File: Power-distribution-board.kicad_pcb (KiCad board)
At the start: 2 copper layers, 137.5 x 119 mm, 98 parts, among them J1 Conn_01x03_Pin, J10 2606-1104/020-000, J11 178.6165.0001, J12 2606-1104/020-000, J14 178.6165.0001, J15 2606-1104/020-000, J16 2606-1104/020-000, J17 178.6165.0001, J18 178.6165.0001, J19 178.6165.0001, J2 2616-1102/020-000, J3 USB_C_Receptacle_USB2.0_14P, J4 178.6165.0001, J5 178.6165.0001, J6 2606-1104/020-000, J8 178.6165.0001, U1 ESP32-S3-WROOM-1, U11 TJA1051TK-3, U12 INA220BIDGSR, U13 INA220BIDGSR, U14 INA220BIDGSR, U15 INA220BIDGSR, U16 INA220BIDGSR, U17 INA220BIDGSR, U3 INA220BIDGSR, U4 CP2102N-Axx-xQFN24, U5 TM1637, U7 INA220BIDGSR, U8 INA220BIDGSR, U9 AP2112K-3.3TRG1

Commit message: fixed pcb issues and added silkscreen edits
fixed long traces breaking up gnd plane
- added designer and reviewer names
- added uva logo and mars logo
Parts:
- added G***: LOGO, LOGO, F.Cu at (183.0, 59.8)
- added G***: LOGO, LOGO, F.Cu at (185.8, 83.4)
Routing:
- net /SCL: track 233.0 -> 271.2 mm, vias 12 -> 4
- net /SDA: track 238.1 -> 250.1 mm, vias 11 -> 13
- net /CLK: track 53.6 -> 57.9 mm, vias 4 -> 6
- net /DIO: track 51.8 -> 53.9 mm
- net /UART TX: track 39.5 -> 40.4 mm, vias 2 -> 4
- net /UART RX: track 36.0 -> 36.9 mm, vias 2 -> 6
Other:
- board text added: "Designed by Josalin Wang Reviewed by Hazel Chen, Aryan Tadepalli, Jayrady Sok"
- board text added: "Power Distribution Board v1 Mechatronics and Robotics Society"
- board text removed: "University of Virginia Mechatronics and Robotics Society"

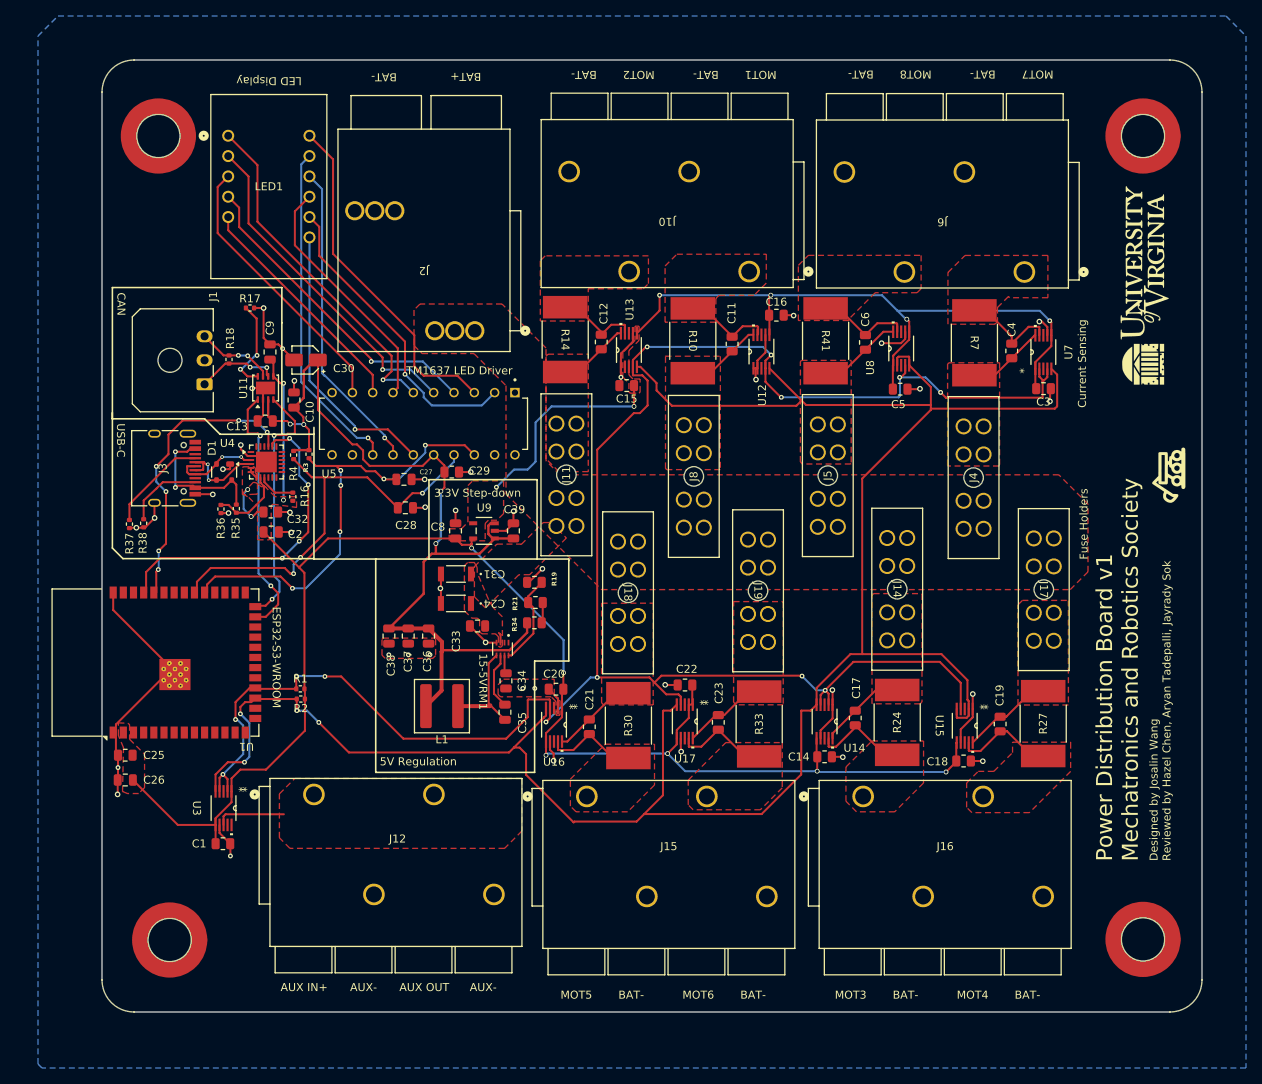
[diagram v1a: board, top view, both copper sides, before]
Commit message: final changes
resolved all DRC errors
-fixed courtyard footprint wago errors
-extended left side more so more space
-rerouted differential traces
-fixed motor pours lol
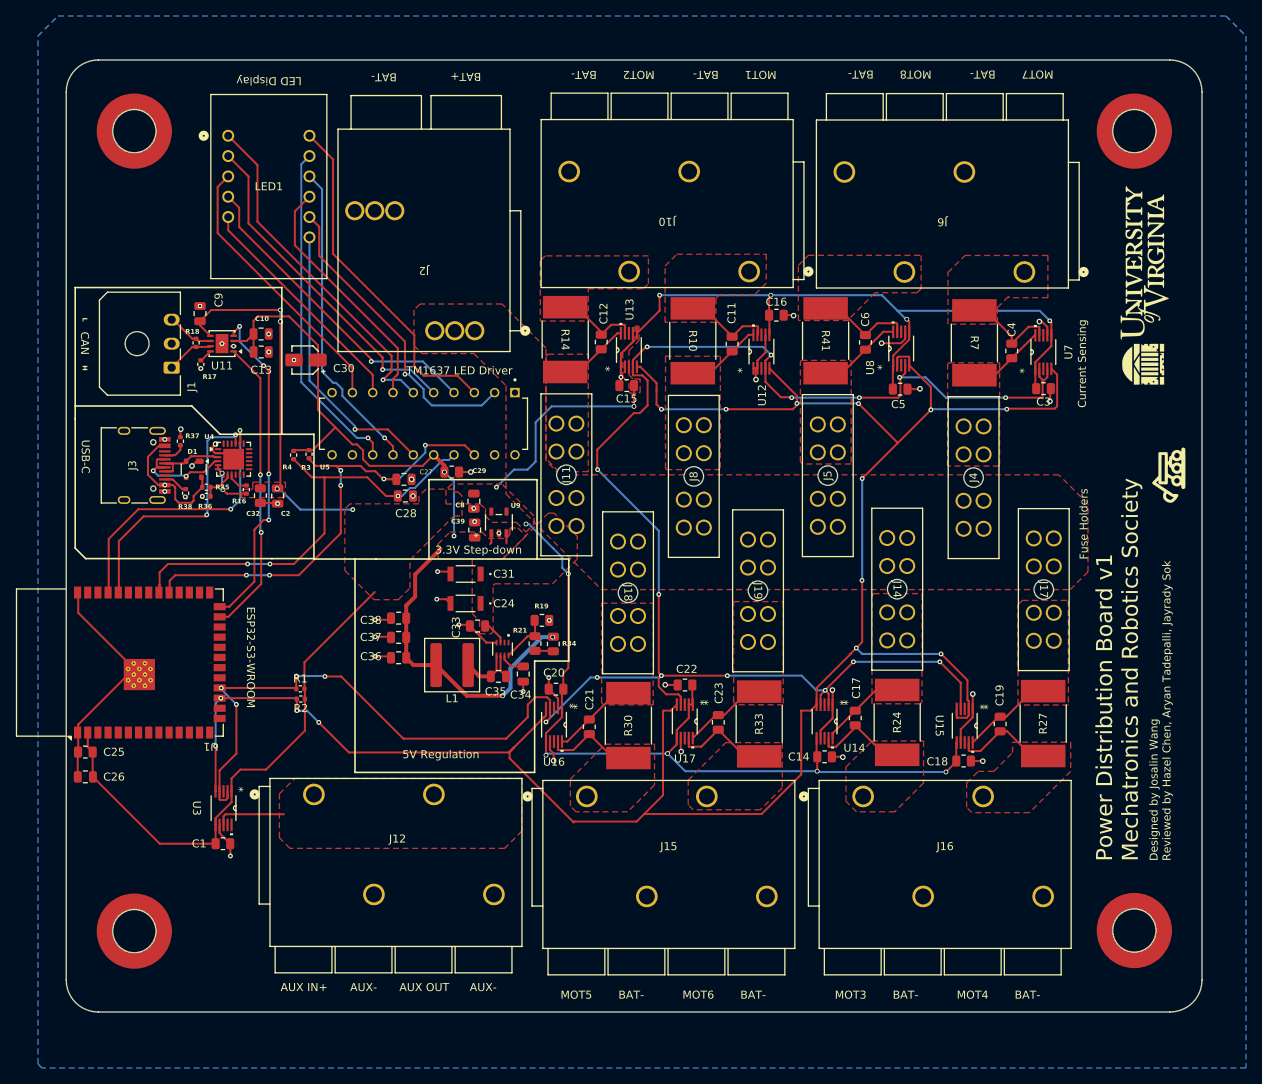
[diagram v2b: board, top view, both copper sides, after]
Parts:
- moved R37 12.2 mm to (62.3, 79.2), turned to 90 degrees
- moved C9 9.98 mm to (64.8, 63.2)
- moved R17 9.36 mm to (64.8, 69.5), turned to -90 degrees
- moved C10 9.22 mm to (72.4, 65.8), turned to 180 degrees
- moved C13 8.64 mm to (72.4, 68.0), turned to 0 degrees
- moved U11 7.78 mm to (67.5, 67.0), turned to 180 degrees
- moved R38 6.45 mm to (63.0, 85.7)
- moved R16 5.87 mm to (70.5, 85.2)
- moved L1 5.29 mm to (96.3, 107.1)
- moved R21 5.13 mm to (106.6, 104.4), turned to 90 degrees
- moved C25 5.01 mm to (50.4, 118.0)
- moved C26 5.01 mm to (50.4, 121.1)
- moved R19 4.85 mm to (107.5, 101.5), turned to 180 degrees
- moved C39 4.85 mm to (99.1, 90.2)
- moved C36 4.63 mm to (89.6, 106.2), turned to 180 degrees
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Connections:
- C35 pad 1: Net-(15-5VRM1-BST) -> Net-(15-5VRM1-SW)
- C35 pad 2: Net-(15-5VRM1-SW) -> Net-(15-5VRM1-BST)
- R18 pad 1: Net-(J1-Pin_3) -> Net-(J1-Pin_1)
- R18 pad 2: Net-(J1-Pin_1) -> Net-(J1-Pin_3)
- U11 pad 6: Net-(J1-Pin_1) -> Net-(J1-Pin_3)
- U11 pad 7: Net-(J1-Pin_3) -> Net-(J1-Pin_1)
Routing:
- net GND: track 142.1 -> 112.6 mm, vias 42 -> 45
- net /5V: track 115.3 -> 104.1 mm
- net Net-(U11-S): track 11.9 -> 1.66 mm, vias 2 -> 0
- net /CAN RX: track 31.4 -> 41.6 mm, vias 2 -> 4
- net /CC1: track 12.6 -> 2.82 mm
- net /3.3V: track 320.6 -> 329.6 mm, vias 16 -> 18
- net Net-(15-5VRM1-SW): track 14.6 -> 6.34 mm
- net /CC2: track 9.70 -> 3.10 mm
- net /SDA: track 250.1 -> 256.6 mm, vias 13 -> 19
- net /CAN TX: track 31.8 -> 37.3 mm
- net Net-(15-5VRM1-FB): track 11.6 -> 6.31 mm
- net Net-(U4-VBUS): track 9.23 -> 4.18 mm
- net /UART TX: track 40.4 -> 35.6 mm, vias 4 -> 2
- net Net-(J1-Pin_1): track 10.2 -> 5.95 mm, vias 2 -> 0
- net Net-(15-5VRM1-BST): track 7.06 -> 2.91 mm
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- added copper zone on F.Cu, net /5V
- removed copper zone on F.Cu, net GND
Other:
- board size 137.5 x 119 mm -> 142 x 119 mm
- board text added: "H"
- board text added: "L"
